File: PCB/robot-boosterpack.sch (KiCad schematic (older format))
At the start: 12 parts

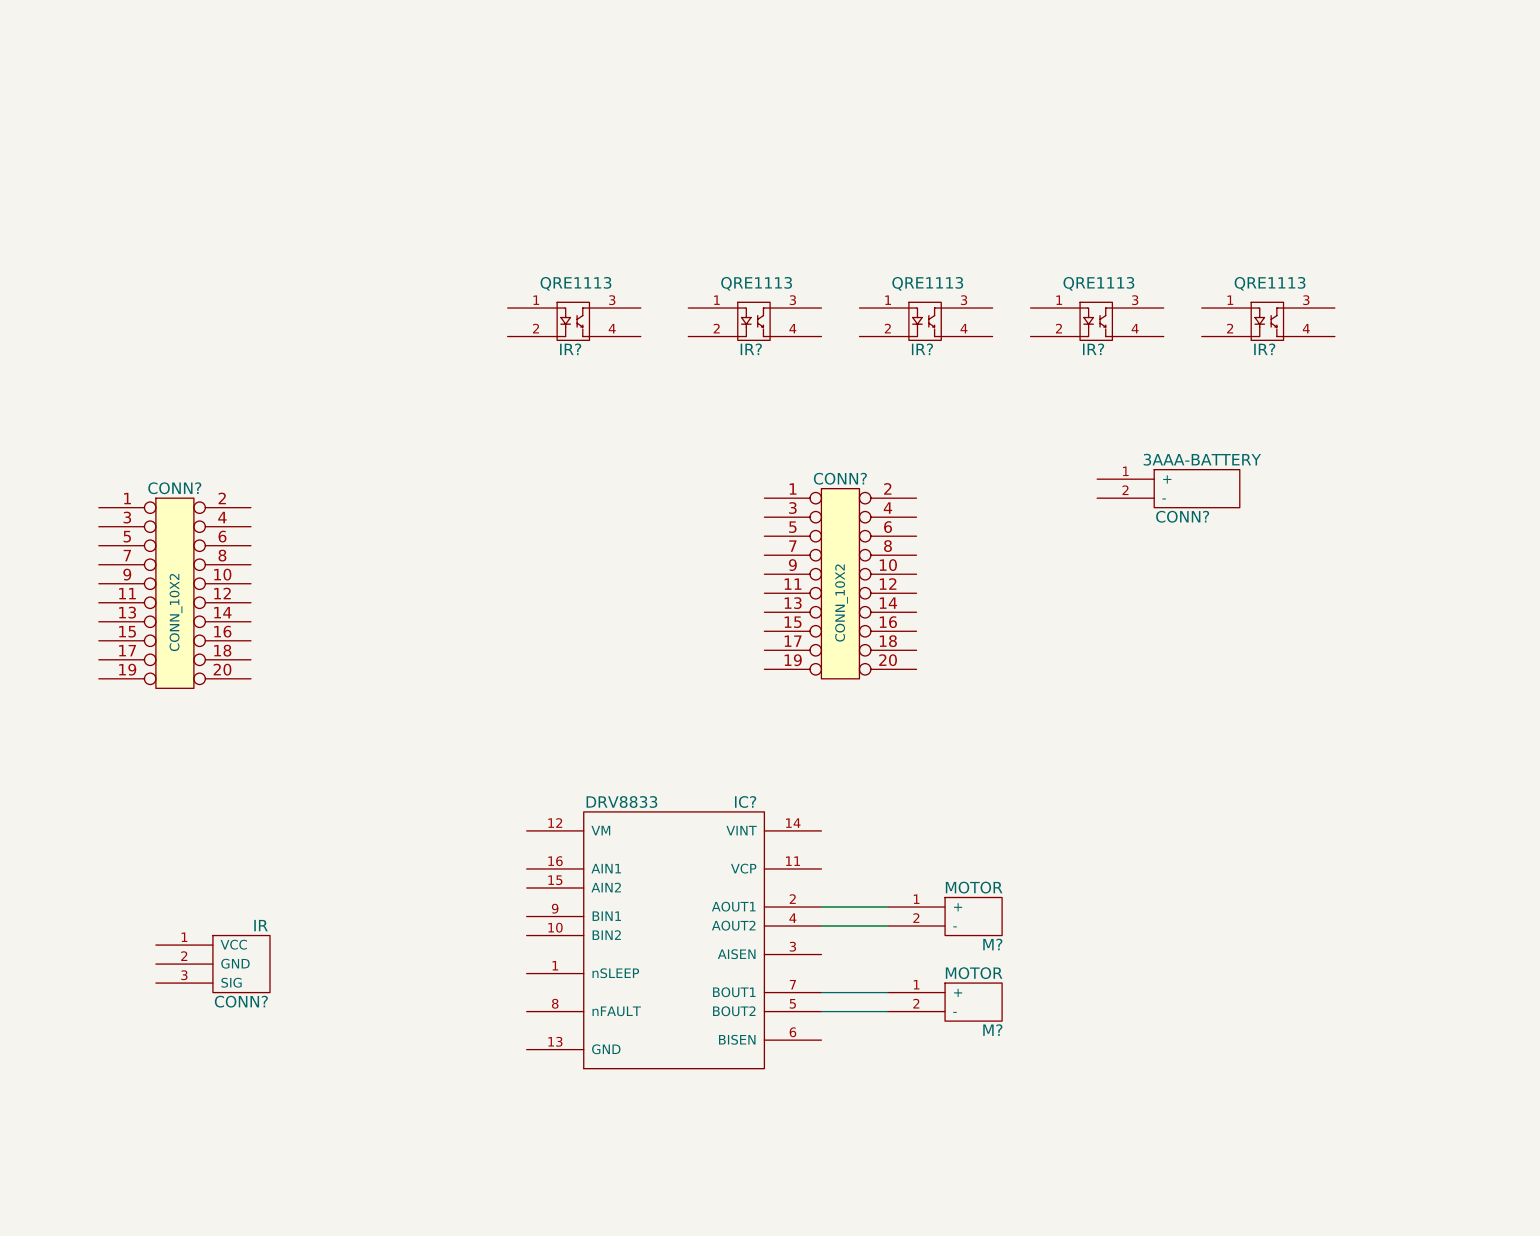
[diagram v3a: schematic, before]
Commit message: fixed grid alignment on reflectance sensor
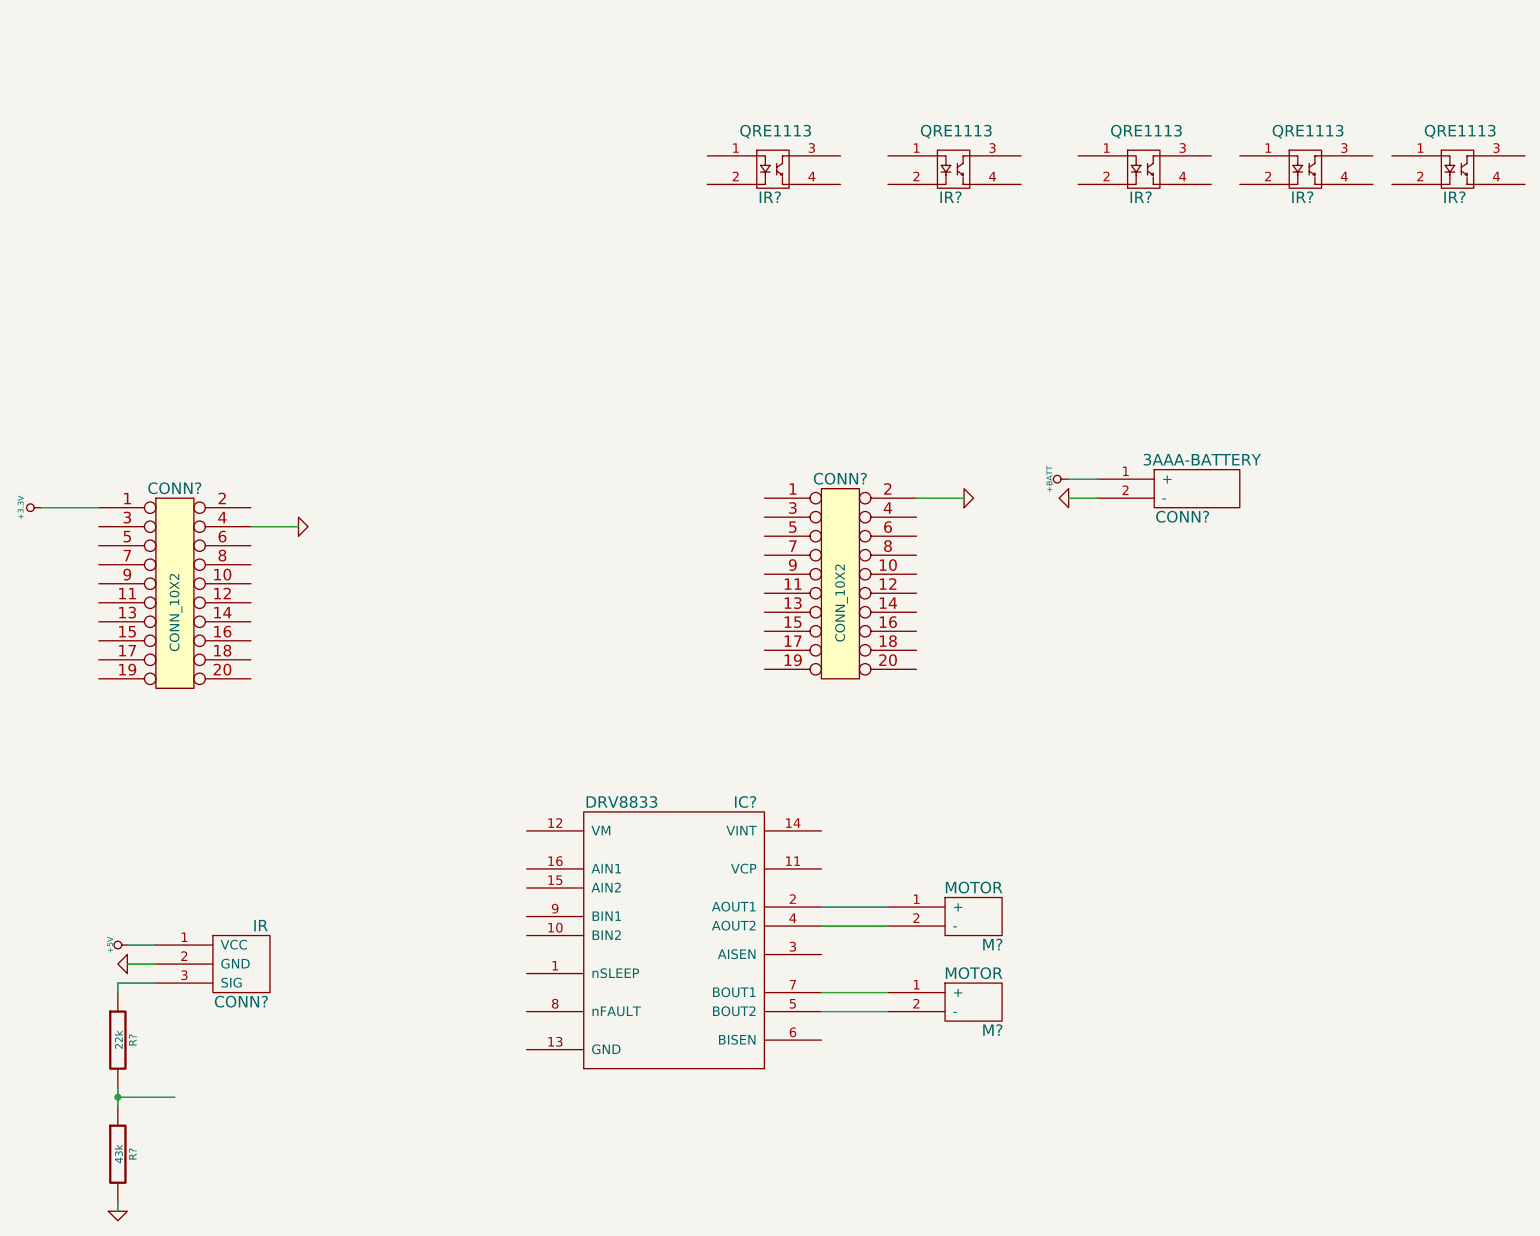
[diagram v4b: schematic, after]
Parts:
- removed IR? (x5): QRE1113, symbol QRE1113
- added IR? (x5): QRE1113, ~, symbol QRE1113
- added R?: 22k, ~, symbol R
- added R?: 43k, ~, symbol R
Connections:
- net labels added: +3.3V, +5V, +BATT, GND
- wire segments 4 -> 16
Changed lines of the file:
@@
 Sheet 1 1
 Title ""
-Date "22 jun 2014"
+Date "23 jun 2014"
 Rev ""
 Comp ""
@@
 $EndComp
 $Comp
-L QRE1113 IR?
-U 1 1 53A7351D
-P 6100 2150
-F 0 "IR?" H 6080 1980 60  0000 C CNN
-F 1 "QRE1113" H 6110 2330 60  0000 C CNN
-F 2 "" H 6110 2330 60  0000 C CNN
-F 3 "" H 6110 2330 60  0000 C CNN
-	1    6100 2150
-	1    0    0    -1
-$EndComp
-$Comp
-L QRE1113 IR?
-U 1 1 53A7352C
-P 7050 2150
-F 0 "IR?" H 7030 1980 60  0000 C CNN
-F 1 "QRE1113" H 7060 2330 60  0000 C CNN
-F 2 "" H 7060 2330 60  0000 C CNN
-F 3 "" H 7060 2330 60  0000 C CNN
-	1    7050 2150
-	1    0    0    -1
-$EndComp
-$Comp
-L QRE1113 IR?
-U 1 1 53A7353B
-P 7950 2150
-F 0 "IR?" H 7930 1980 60  0000 C CNN
-F 1 "QRE1113" H 7960 2330 60  0000 C CNN
-F 2 "" H 7960 2330 60  0000 C CNN
-F 3 "" H 7960 2330 60  0000 C CNN
-	1    7950 2150
-	1    0    0    -1
-$EndComp
-$Comp
-L QRE1113 IR?
-U 1 1 53A7354A
-P 8850 2150
-F 0 "IR?" H 8830 1980 60  0000 C CNN
-F 1 "QRE1113" H 8860 2330 60  0000 C CNN
-F 2 "" H 8860 2330 60  0000 C CNN
-F 3 "" H 8860 2330 60  0000 C CNN
-	1    8850 2150
-	1    0    0    -1
-$EndComp
-$Comp
-L QRE1113 IR?
-U 1 1 53A73559
-P 9750 2150
-F 0 "IR?" H 9730 1980 60  0000 C CNN
-F 1 "QRE1113" H 9760 2330 60  0000 C CNN
-F 2 "" H 9760 2330 60  0000 C CNN
-F 3 "" H 9760 2330 60  0000 C CNN
-	1    9750 2150
-	1    0    0    -1
-$EndComp
-Wire Wire Line
-	7400 5250 7750 5250
-Wire Wire Line
-	7400 5350 7750 5350
-Wire Wire Line
-	7400 5700 7750 5700
-Wire Wire Line
-	7400 5800 7750 5800
-$Comp
 L 3AAA-BATTERY CONN?
 U 1 1 53A73812
@@
 	1    0    0    -1
 $EndComp
+$Comp
+L +3.3V #PWR?
+U 1 1 53A7389D
+P 3300 3150
+F 0 "#PWR?" H 3300 3110 30  0001 C CNN
+F 1 "+3.3V" H 3300 3260 30  0000 C CNN
+F 2 "" H 3300 3150 60  0000 C CNN
+F 3 "" H 3300 3150 60  0000 C CNN
+	1    3300 3150
+	0    -1   -1   0
+$EndComp
+$Comp
+L GND #PWR?
+U 1 1 53A738AC
+P 4650 3250
+F 0 "#PWR?" H 4650 3250 30  0001 C CNN
+F 1 "GND" H 4650 3180 30  0001 C CNN
+F 2 "" H 4650 3250 60  0000 C CNN
+F 3 "" H 4650 3250 60  0000 C CNN
+	1    4650 3250
+	0    -1   -1   0
+$EndComp
+$Comp
+L GND #PWR?
+U 1 1 53A73A8C
+P 8150 3100
+F 0 "#PWR?" H 8150 3100 30  0001 C CNN
+F 1 "GND" H 8150 3030 30  0001 C CNN
+F 2 "" H 8150 3100 60  0000 C CNN
+F 3 "" H 8150 3100 60  0000 C CNN
+	1    8150 3100
+	0    -1   -1   0
+$EndComp
+$Comp
+L GND #PWR?
+U 1 1 53A73AA3
+P 8700 3100
+F 0 "#PWR?" H 8700 3100 30  0001 C CNN
+F 1 "GND" H 8700 3030 30  0001 C CNN
+F 2 "" H 8700 3100 60  0000 C CNN
+F 3 "" H 8700 3100 60  0000 C CNN
+	1    8700 3100
+	0    1    1    0
+$EndComp
+$Comp
+L +5V #PWR?
+U 1 1 53A73BE8
+P 3750 5450
+F 0 "#PWR?" H 3750 5540 20  0001 C CNN
+F 1 "+5V" H 3750 5540 30  0000 C CNN
+F 2 "" H 3750 5450 60  0000 C CNN
+F 3 "" H 3750 5450 60  0000 C CNN
+	1    3750 5450
+	0    -1   -1   0
+$EndComp
+$Comp
+L GND #PWR?
+U 1 1 53A73C0D
+P 3750 5550
+F 0 "#PWR?" H 3750 5550 30  0001 C CNN
+F 1 "GND" H 3750 5480 30  0001 C CNN
+F 2 "" H 3750 5550 60  0000 C CNN
+F 3 "" H 3750 5550 60  0000 C CNN
+	1    3750 5550
+	0    1    1    0
+$EndComp
+$Comp
+L R R?
+U 1 1 53A7892C
+P 3700 5950
+F 0 "R?" V 3780 5950 40  0000 C CNN
+F 1 "22k" V 3707 5951 40  0000 C CNN
+F 2 "~" V 3630 5950 30  0000 C CNN
+F 3 "~" H 3700 5950 30  0000 C CNN
+	1    3700 5950
+	1    0    0    -1
+$EndComp
+$Comp
+L R R?
+U 1 1 53A78939
+P 3700 6550
+F 0 "R?" V 3780 6550 40  0000 C CNN
+F 1 "43k" V 3707 6551 40  0000 C CNN
+F 2 "~" V 3630 6550 30  0000 C CNN
+F 3 "~" H 3700 6550 30  0000 C CNN
+	1    3700 6550
+	1    0    0    -1
+$EndComp
+Wire Wire Line
+	7400 5250 7750 5250
+Wire Wire Line
+	7400 5350 7750 5350
+Wire Wire Line
+	7400 5700 7750 5700
+Wire Wire Line
+	7400 5800 7750 5800
+Wire Wire Line
+	4400 3250 4650 3250
+Wire Wire Line
+	3300 3150 3600 3150
+Wire Wire Line
+	7900 3100 8150 3100
+Wire Wire Line
+	8850 3100 8700 3100
+Wire Wire Line
+	3900 5450 3750 5450
+Wire Wire Line
+	3900 5550 3750 5550
+Wire Wire Line
+	3900 5650 3700 5650
+Wire Wire Line
+	3700 5650 3700 5700
+Wire Wire Line
+	3700 6200 3700 6300
+$Comp
+L GND #PWR?
+U 1 1 53A7897C
+P 3700 6850
+F 0 "#PWR?" H 3700 6850 30  0001 C CNN
+F 1 "GND" H 3700 6780 30  0001 C CNN
+F 2 "" H 3700 6850 60  0000 C CNN
+F 3 "" H 3700 6850 60  0000 C CNN
+	1    3700 6850
+	1    0    0    -1
+$EndComp
+Wire Wire Line
+	3700 6850 3700 6800
+Wire Wire Line
+	3700 6250 4000 6250
+Connection ~ 3700 6250
+$Comp
+L QRE1113 IR?
+U 1 1 53A78E80
+P 7150 1350
+F 0 "IR?" H 7130 1180 60  0000 C CNN
+F 1 "QRE1113" H 7160 1530 60  0000 C CNN
+F 2 "~" H 7160 1530 60  0000 C CNN
+F 3 "~" H 7160 1530 60  0000 C CNN
+	1    7150 1350
+	1    0    0    -1
+$EndComp
+$Comp
+L QRE1113 IR?
+U 1 1 53A78E8D
+P 8100 1350
+F 0 "IR?" H 8080 1180 60  0000 C CNN
+F 1 "QRE1113" H 8110 1530 60  0000 C CNN
+F 2 "~" H 8110 1530 60  0000 C CNN
+F 3 "~" H 8110 1530 60  0000 C CNN
+	1    8100 1350
+	1    0    0    -1
+$EndComp
+$Comp
+L QRE1113 IR?
+U 1 1 53A78E93
+P 9100 1350
+F 0 "IR?" H 9080 1180 60  0000 C CNN
+F 1 "QRE1113" H 9110 1530 60  0000 C CNN
+F 2 "~" H 9110 1530 60  0000 C CNN
+F 3 "~" H 9110 1530 60  0000 C CNN
+	1    9100 1350
+	1    0    0    -1
+$EndComp
+$Comp
+L QRE1113 IR?
+U 1 1 53A78E99
+P 9950 1350
+F 0 "IR?" H 9930 1180 60  0000 C CNN
+F 1 "QRE1113" H 9960 1530 60  0000 C CNN
+F 2 "~" H 9960 1530 60  0000 C CNN
+F 3 "~" H 9960 1530 60  0000 C CNN
+	1    9950 1350
+	1    0    0    -1
+$EndComp
+$Comp
+L QRE1113 IR?
+U 1 1 53A78E9F
+P 10750 1350
+F 0 "IR?" H 10730 1180 60  0000 C CNN
+F 1 "QRE1113" H 10760 1530 60  0000 C CNN
+F 2 "~" H 10760 1530 60  0000 C CNN
+F 3 "~" H 10760 1530 60  0000 C CNN
+	1    10750 1350
+	1    0    0    -1
+$EndComp
+$Comp
+L +BATT #PWR?
+U 1 1 53A78F53
+P 8700 3000
+F 0 "#PWR?" H 8700 2950 20  0001 C CNN
+F 1 "+BATT" H 8700 3100 30  0000 C CNN
+F 2 "" H 8700 3000 60  0000 C CNN
+F 3 "" H 8700 3000 60  0000 C CNN
+	1    8700 3000
+	0    -1   -1   0
+$EndComp
+Wire Wire Line
+	8850 3000 8700 3000
 $EndSCHEMATC

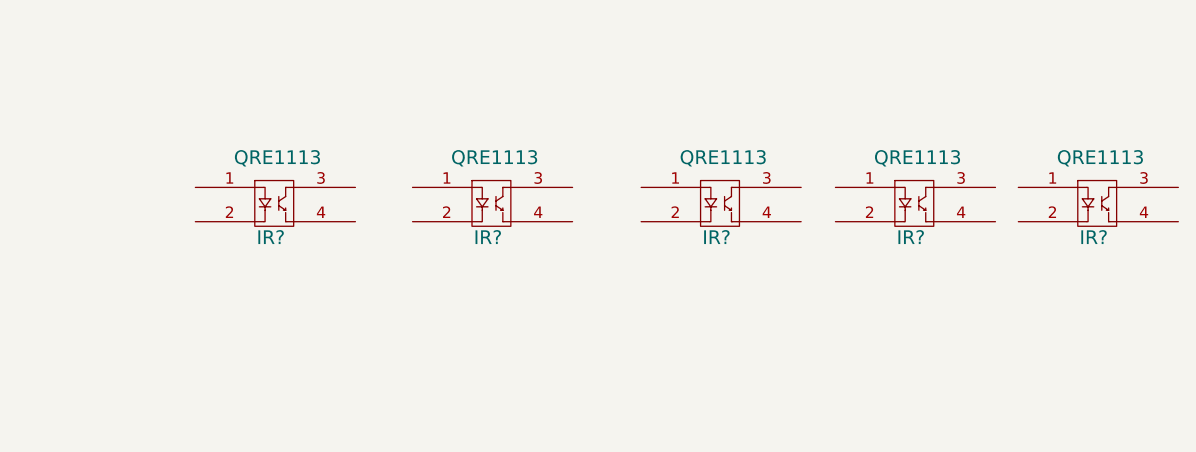
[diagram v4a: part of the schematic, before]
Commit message: created reflectance sensor circuit
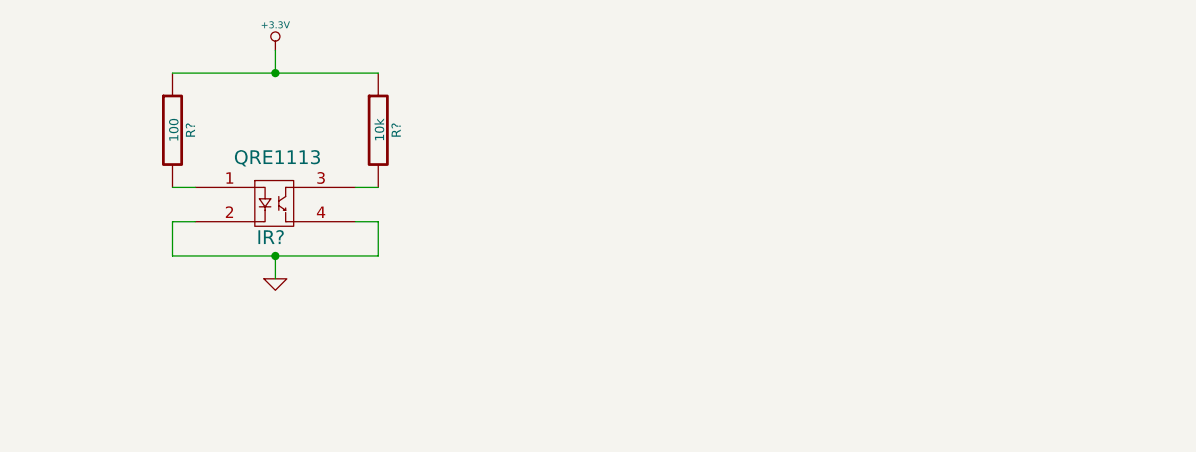
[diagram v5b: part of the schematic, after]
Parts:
- removed IR? (x4): QRE1113, ~, symbol QRE1113
- added R?: 100, ~, symbol R
- added R?: 10k, ~, symbol R
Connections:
- wire segments 16 -> 26
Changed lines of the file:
@@
-$EndComp
-$Comp
-L QRE1113 IR?
-U 1 1 53A78E8D
-P 8100 1350
-F 0 "IR?" H 8080 1180 60  0000 C CNN
-F 1 "QRE1113" H 8110 1530 60  0000 C CNN
-F 2 "~" H 8110 1530 60  0000 C CNN
-F 3 "~" H 8110 1530 60  0000 C CNN
-	1    8100 1350
-	1    0    0    -1
-$EndComp
-$Comp
-L QRE1113 IR?
-U 1 1 53A78E93
-P 9100 1350
-F 0 "IR?" H 9080 1180 60  0000 C CNN
-F 1 "QRE1113" H 9110 1530 60  0000 C CNN
-F 2 "~" H 9110 1530 60  0000 C CNN
-F 3 "~" H 9110 1530 60  0000 C CNN
-	1    9100 1350
-	1    0    0    -1
-$EndComp
-$Comp
-L QRE1113 IR?
-U 1 1 53A78E99
-P 9950 1350
-F 0 "IR?" H 9930 1180 60  0000 C CNN
-F 1 "QRE1113" H 9960 1530 60  0000 C CNN
-F 2 "~" H 9960 1530 60  0000 C CNN
-F 3 "~" H 9960 1530 60  0000 C CNN
-	1    9950 1350
-	1    0    0    -1
-$EndComp
-$Comp
-L QRE1113 IR?
-U 1 1 53A78E9F
-P 10750 1350
-F 0 "IR?" H 10730 1180 60  0000 C CNN
-F 1 "QRE1113" H 10760 1530 60  0000 C CNN
-F 2 "~" H 10760 1530 60  0000 C CNN
-F 3 "~" H 10760 1530 60  0000 C CNN
-	1    10750 1350
-	1    0    0    -1
 $EndComp
 $Comp
@@
 Wire Wire Line
 	8850 3000 8700 3000
+$Comp
+L R R?
+U 1 1 53A79029
+P 6700 1050
+F 0 "R?" V 6780 1050 40  0000 C CNN
+F 1 "100" V 6707 1051 40  0000 C CNN
+F 2 "~" V 6630 1050 30  0000 C CNN
+F 3 "~" H 6700 1050 30  0000 C CNN
+	1    6700 1050
+	1    0    0    -1
+$EndComp
+Wire Wire Line
+	6800 1300 6700 1300
+Wire Wire Line
+	6800 1450 6700 1450
+Wire Wire Line
+	6700 1450 6700 1600
+$Comp
+L +3.3V #PWR?
+U 1 1 53A7905A
+P 7150 700
+F 0 "#PWR?" H 7150 660 30  0001 C CNN
+F 1 "+3.3V" H 7150 810 30  0000 C CNN
+F 2 "" H 7150 700 60  0000 C CNN
+F 3 "" H 7150 700 60  0000 C CNN
+	1    7150 700
+	1    0    0    -1
+$EndComp
+$Comp
+L GND #PWR?
+U 1 1 53A7907B
+P 7150 1700
+F 0 "#PWR?" H 7150 1700 30  0001 C CNN
+F 1 "GND" H 7150 1630 30  0001 C CNN
+F 2 "" H 7150 1700 60  0000 C CNN
+F 3 "" H 7150 1700 60  0000 C CNN
+	1    7150 1700
+	1    0    0    -1
+$EndComp
+Wire Wire Line
+	7500 1450 7600 1450
+$Comp
+L R R?
+U 1 1 53A790C7
+P 7600 1050
+F 0 "R?" V 7680 1050 40  0000 C CNN
+F 1 "10k" V 7607 1051 40  0000 C CNN
+F 2 "~" V 7530 1050 30  0000 C CNN
+F 3 "~" H 7600 1050 30  0000 C CNN
+	1    7600 1050
+	1    0    0    -1
+$EndComp
+Wire Wire Line
+	7500 1300 7600 1300
+Wire Wire Line
+	6700 800  7600 800
+Wire Wire Line
+	7150 800  7150 700
+Connection ~ 7150 800
+Wire Wire Line
+	7600 1450 7600 1600
+Wire Wire Line
+	7600 1600 6700 1600
+Wire Wire Line
+	7150 1700 7150 1600
+Connection ~ 7150 1600
 $EndSCHEMATC
